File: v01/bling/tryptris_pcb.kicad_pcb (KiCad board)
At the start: 2 copper layers, 298.8 x 122 mm, 227 parts, among them J1 USB_C_Receptacle_USB2.0, J2 I2C-L, J3 I2C-R, J4 AVR-ISP-6, SW1 Reset, U1 ATmega32U4-AU, U2 MCP23017_SO, U3 IS31FL3733-TQ, U4 HOLE, U4 IS31FL3733-TQ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

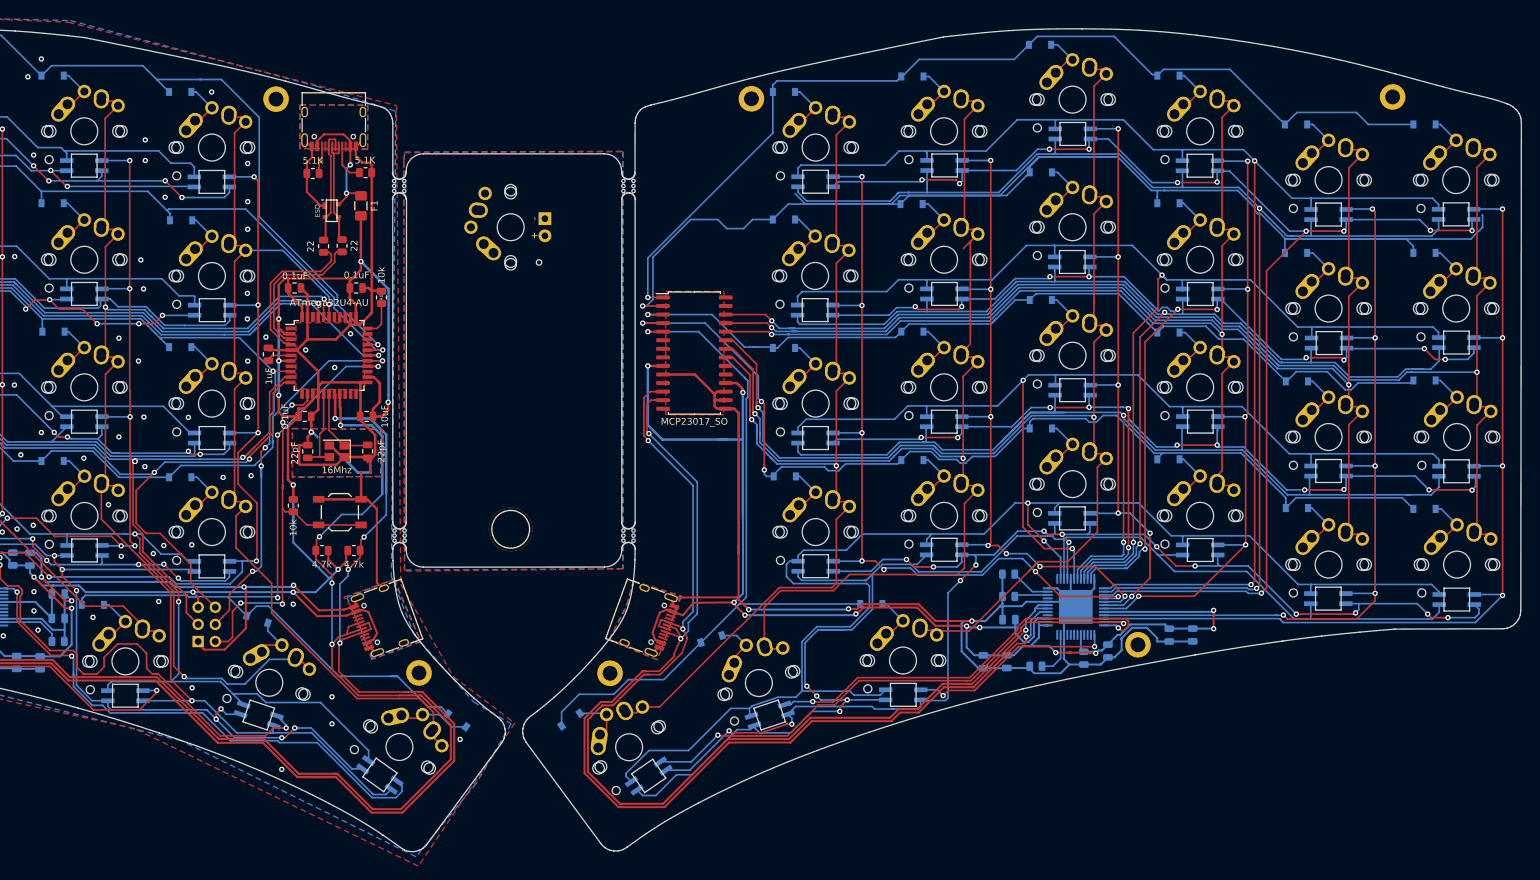
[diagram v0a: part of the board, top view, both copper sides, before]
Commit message: Add more copper fill
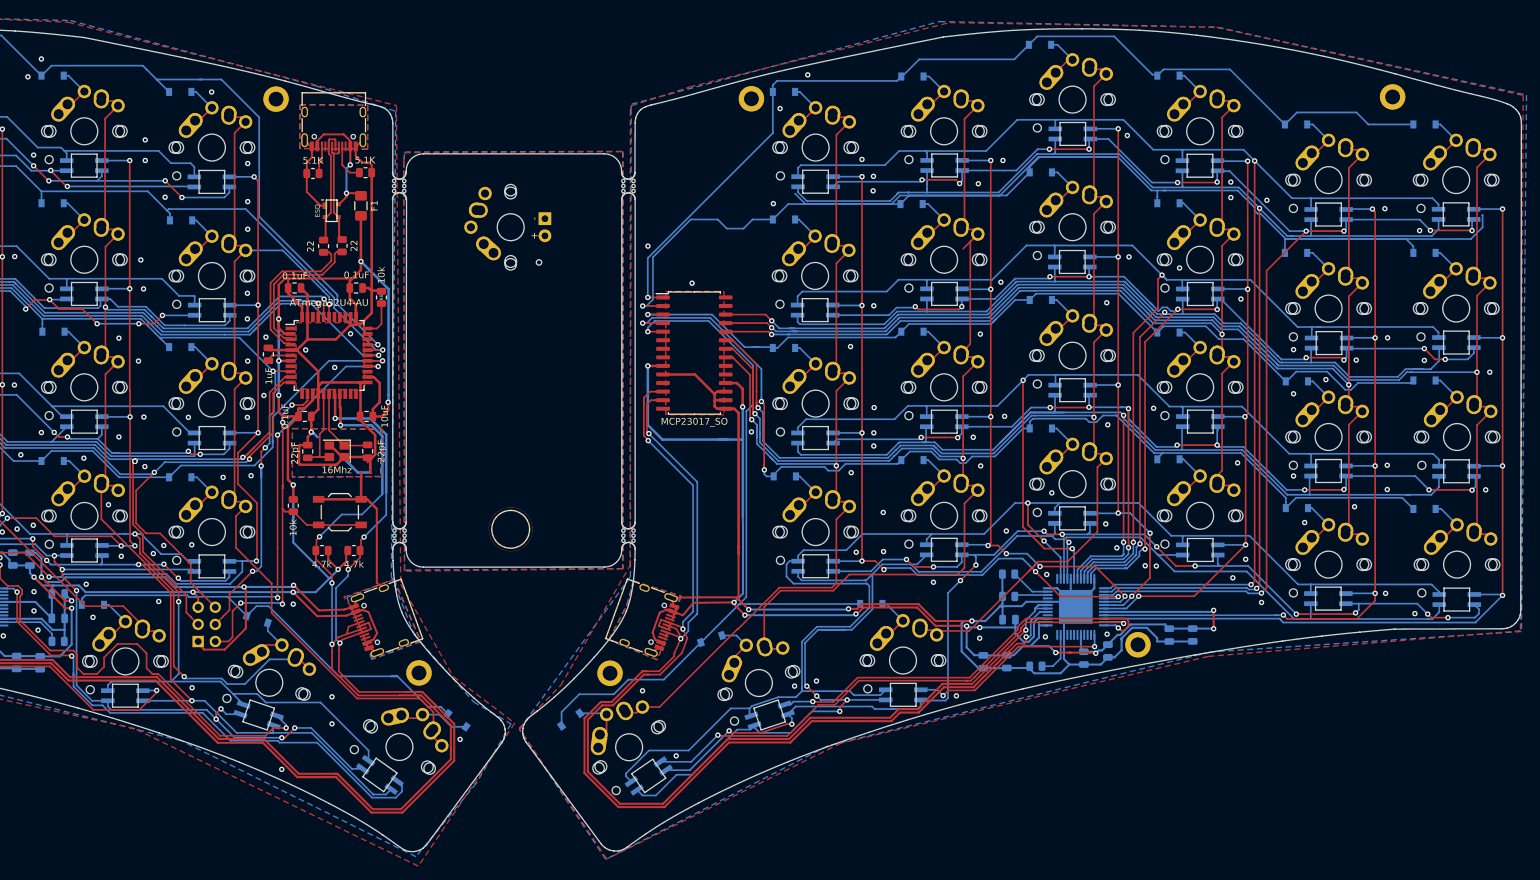
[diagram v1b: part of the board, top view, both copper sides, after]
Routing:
- net Row4-R: track 107.3 -> 111.4 mm
- net Row3-R: track 151.3 -> 152.8 mm
- net GND: track 309.1 -> 309.7 mm, vias 87 -> 89
- net VSS: vias 3 -> 75

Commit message: Improve fill areas for bling.
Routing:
- net Row1-R: track 226.1 -> 153.3 mm
- net GND: track 309.7 -> 313.8 mm, vias 89 -> 92
- net Right-SW3: track 193.6 -> 191.7 mm
- net Right-SW2: track 203.1 -> 204.6 mm
- net Right-CS6: track 135.5 -> 137.0 mm
- net Right-SW11: track 197.5 -> 198.9 mm
- net Row2-L: track 173.1 -> 174.4 mm
- net Left-SW3: track 215.5 -> 216.7 mm
- net Right-SW10: track 196.5 -> 197.5 mm
- net Right-SW4: track 147.1 -> 146.2 mm
- net Left-SW8: track 196.2 -> 197.1 mm
- net Row3-R: track 152.8 -> 153.5 mm
- net Left-SW1: track 252.6 -> 253.2 mm
- net Col9: track 148.0 -> 147.4 mm
- net Net-(J4-Pad5): track 62.1 -> 61.5 mm
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
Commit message: Add ESD circuits to bling interconnects.
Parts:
- added U6: PRTR5V0U2X, Keebio-Parts:SOT-143B, F.Cu at (149.7, 118.0)
- added U7: PRTR5V0U2X, Keebio-Parts:SOT-143B, F.Cu at (202.6, 118.2)
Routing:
- net VSS: track 190.8 -> 143.2 mm
- net SDA-R: track 162.3 -> 174.2 mm
- net SCL-R: track 163.1 -> 174.4 mm
- net SCL-L: track 178.2 -> 184.5 mm
- net SDA-L: track 172.8 -> 179.0 mm
- net VBUS: track 209.4 -> 213.3 mm
- net +5V: track 268.6 -> 272.2 mm
- net Col6: track 151.1 -> 154.5 mm
- net Row4-R: track 111.4 -> 112.9 mm
- net GND: vias 92 -> 91
